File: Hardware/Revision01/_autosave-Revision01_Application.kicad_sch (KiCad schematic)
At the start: 24 parts, among them J11 Conn_02x08_Odd_Even, J13 Conn_02x08_Odd_Even, Q2 PMV32UP,215, Q3 PMV32UP,215, U3 AD7124-8BCPZ-RL7, U6 ICM-45605, U7 MRF89XAM9AT-I/RM

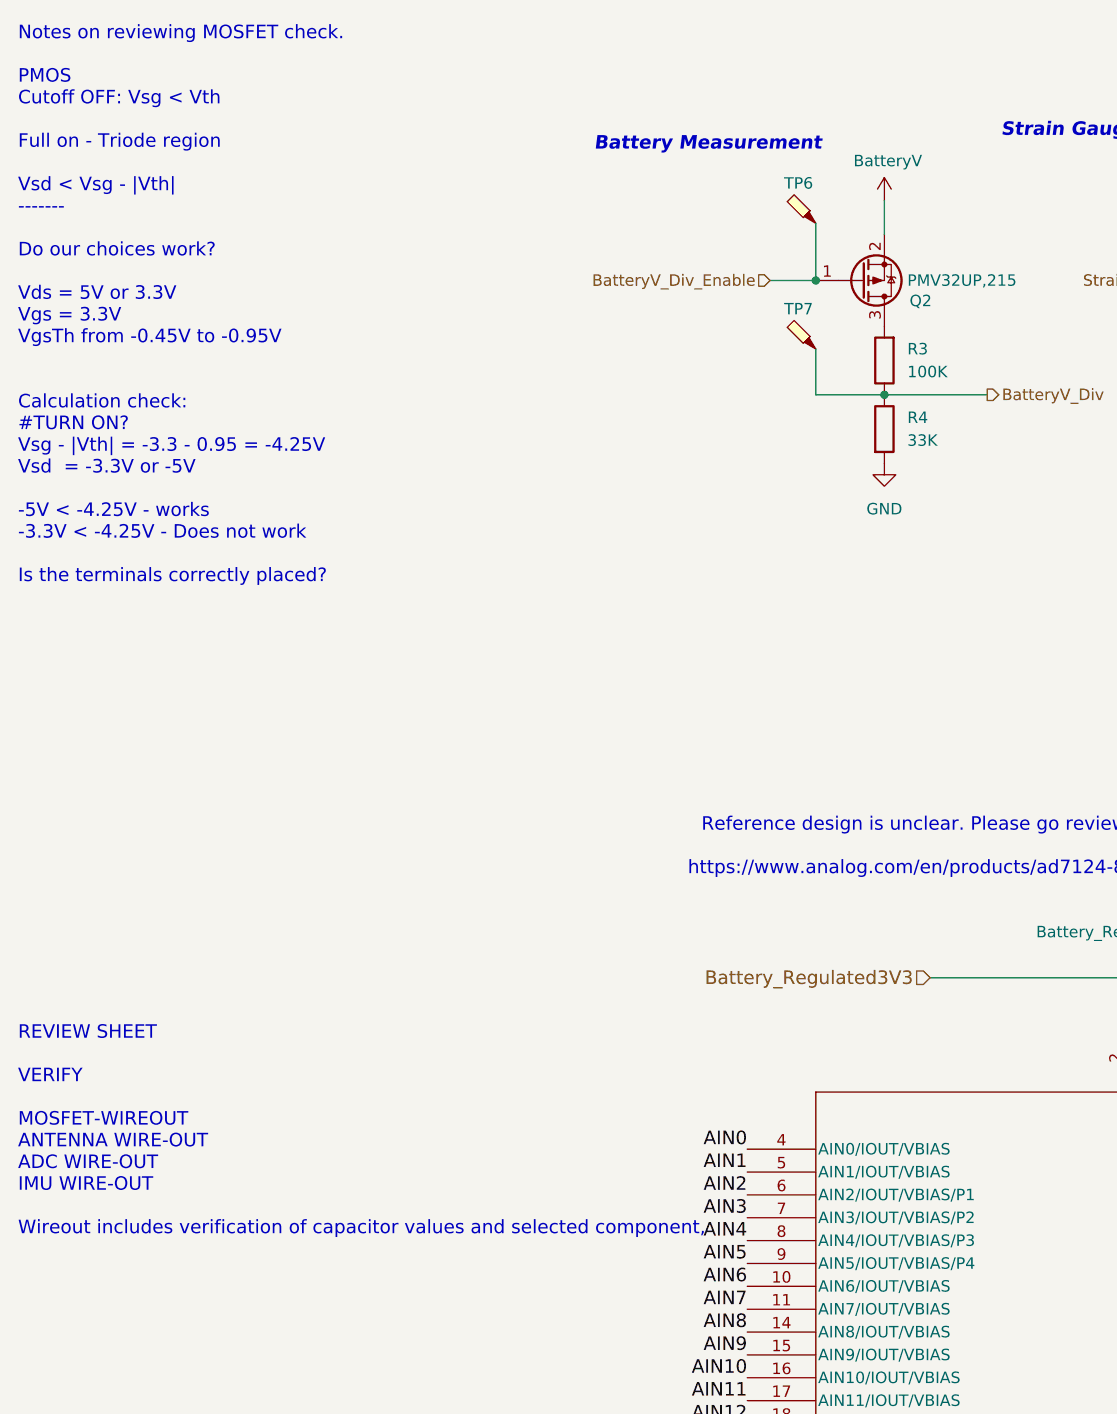
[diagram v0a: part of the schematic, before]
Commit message: redid mosfet calculations, 3.3V switching load should be fine calculations in application sheet
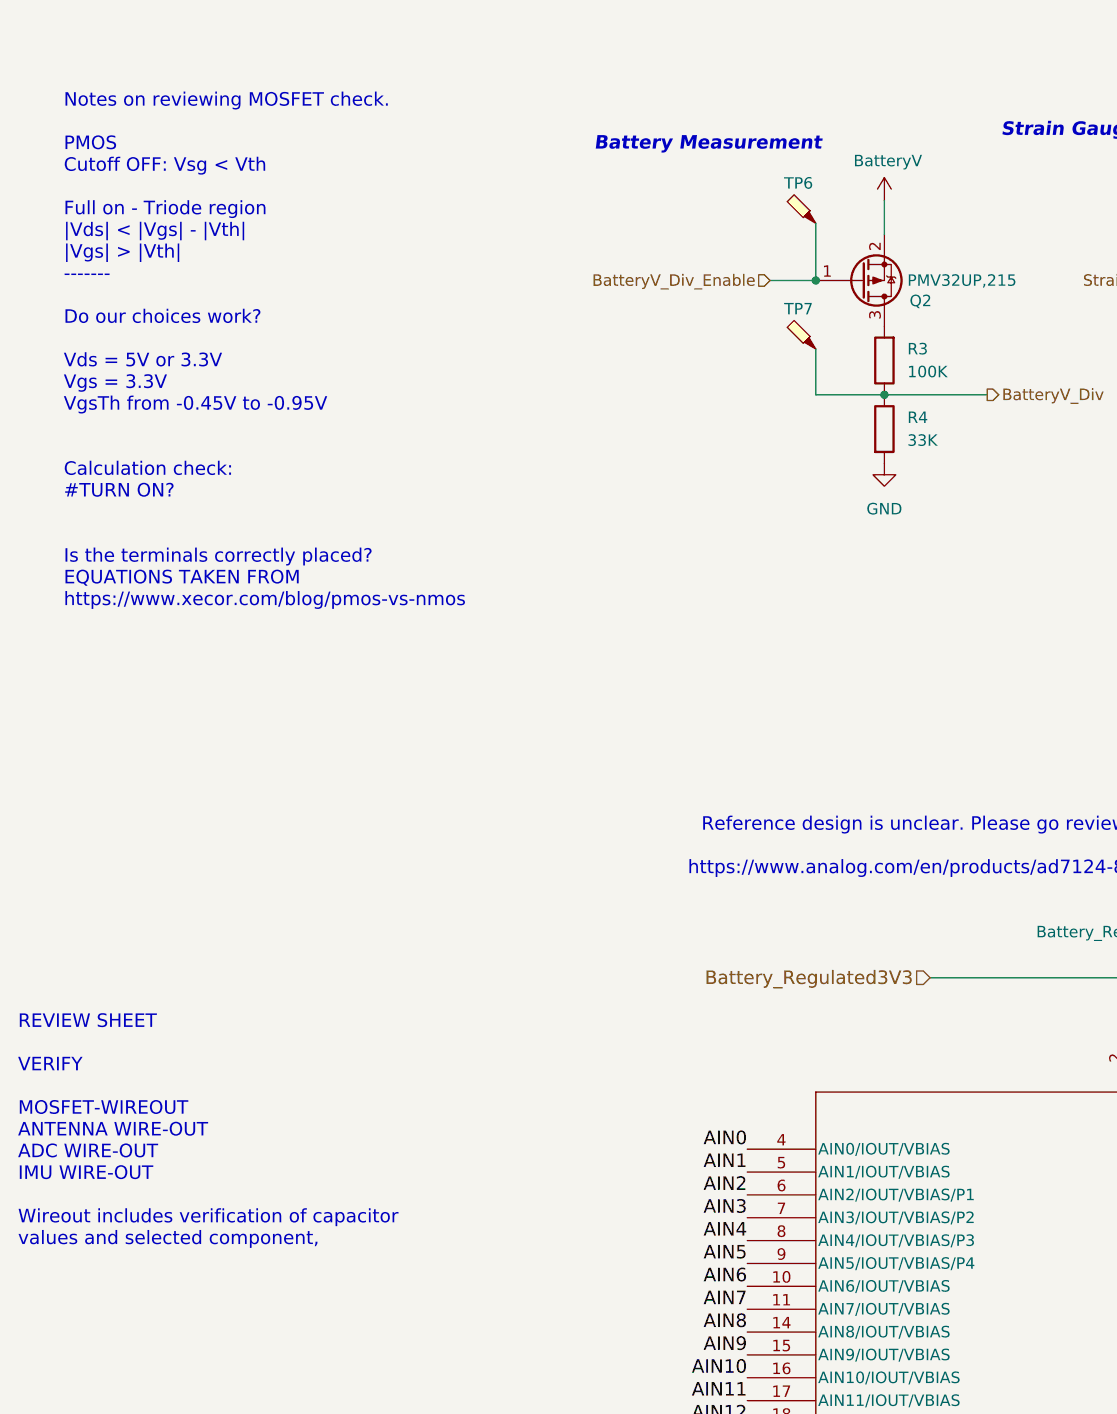
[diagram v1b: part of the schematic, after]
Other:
- note added: "Notes on reviewing MOSFET check. PMOS Cutoff OFF: Vsg < Vth Full on - Triode region |Vds| < |Vgs| - |Vth| |Vgs| > |Vth| ------- Do our choices work? Vds = 5V or 3.3V Vgs = 3.3V VgsTh from -0.45V to -0.95V Calculation check: #TURN ON? Is the terminals correctly placed? EQUATIONS TAKEN FROM https://www.xecor.com/blog/pmos-vs-nmos"
- note removed: "Notes on reviewing MOSFET check. PMOS Cutoff OFF: Vsg < Vth Full on - Triode region Vsd < Vsg - |Vth| ------- Do our choices work? Vds = 5V or 3.3V Vgs = 3.3V VgsTh from -0.45V to -0.95V Calculation check: #TURN ON? Vsg - |Vth| = -3.3 - 0.95 = -4.25V Vsd = -3.3V or -5V -5V < -4.25V - works -3.3V < -4.25V - Does not work Is the terminals correctly placed?"
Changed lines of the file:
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@@
 		)
 	)
-	(text "REVIEW SHEET\n\nVERIFY \n\nMOSFET-WIREOUT\nANTENNA WIRE-OUT\nADC WIRE-OUT\nIMU WIRE-OUT\n\nWireout includes verification of capacitor values and selected component, \n\n"
+	(text "REVIEW SHEET\n\nVERIFY \n\nMOSFET-WIREOUT\nANTENNA WIRE-OUT\nADC WIRE-OUT\nIMU WIRE-OUT\n\nWireout includes verification of capacitor \nvalues and selected component, \n\n"
 		(exclude_from_sim no)
 		(at -48.006 133.858 0)
@@
 		)
 	)
-	(text "Notes on reviewing MOSFET check.\n\nPMOS\nCutoff OFF: Vsg < Vth \n\nFull on - Triode region\n\nVsd < Vsg - |Vth|\n-------\n\nDo our choices work?\n\nVds = 5V or 3.3V\nVgs = 3.3V\nVgsTh from -0.45V to -0.95V\n\n\nCalculation check:\n#TURN ON?\nVsg - |Vth| = -3.3 - 0.95 = -4.25V\nVsd  = -3.3V or -5V\n\n-5V < -4.25V - works\n-3.3V < -4.25V - Does not work\n\nIs the terminals correctly placed?"
+	(text "Notes on reviewing MOSFET check.\n\nPMOS\nCutoff OFF: Vsg < Vth \n\nFull on - Triode region\n|Vds| < |Vgs| - |Vth|\n|Vgs| > |Vth|\n-------\n\nDo our choices work?\n\nVds = 5V or 3.3V\nVgs = 3.3V\nVgsTh from -0.45V to -0.95V\n\n\nCalculation check:\n#TURN ON?\n\n\nIs the terminals correctly placed?\nEQUATIONS TAKEN FROM\nhttps://www.xecor.com/blog/pmos-vs-nmos"
 		(exclude_from_sim no)
-		(at -48.006 40.894 0)
+		(at -42.926 45.974 0)
 		(effects
 			(font
